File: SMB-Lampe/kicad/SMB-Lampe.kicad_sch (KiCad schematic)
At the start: 2 parts, among them P1 USB_C_Plug_USB2.0, SW1 SW_SPST

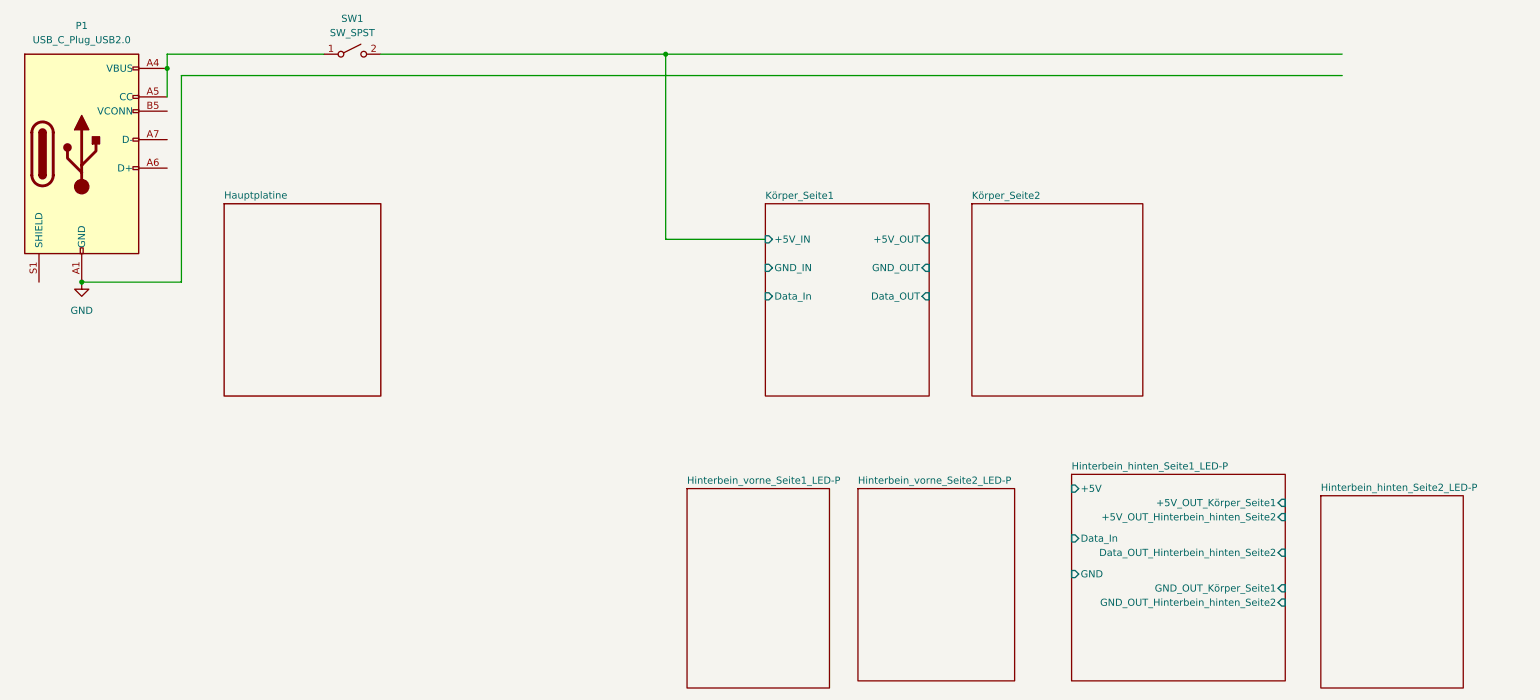
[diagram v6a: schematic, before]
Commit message: Vorderseite Platine Körper Seite 1 fertig
zwei GND Verbindungen fehlen noch
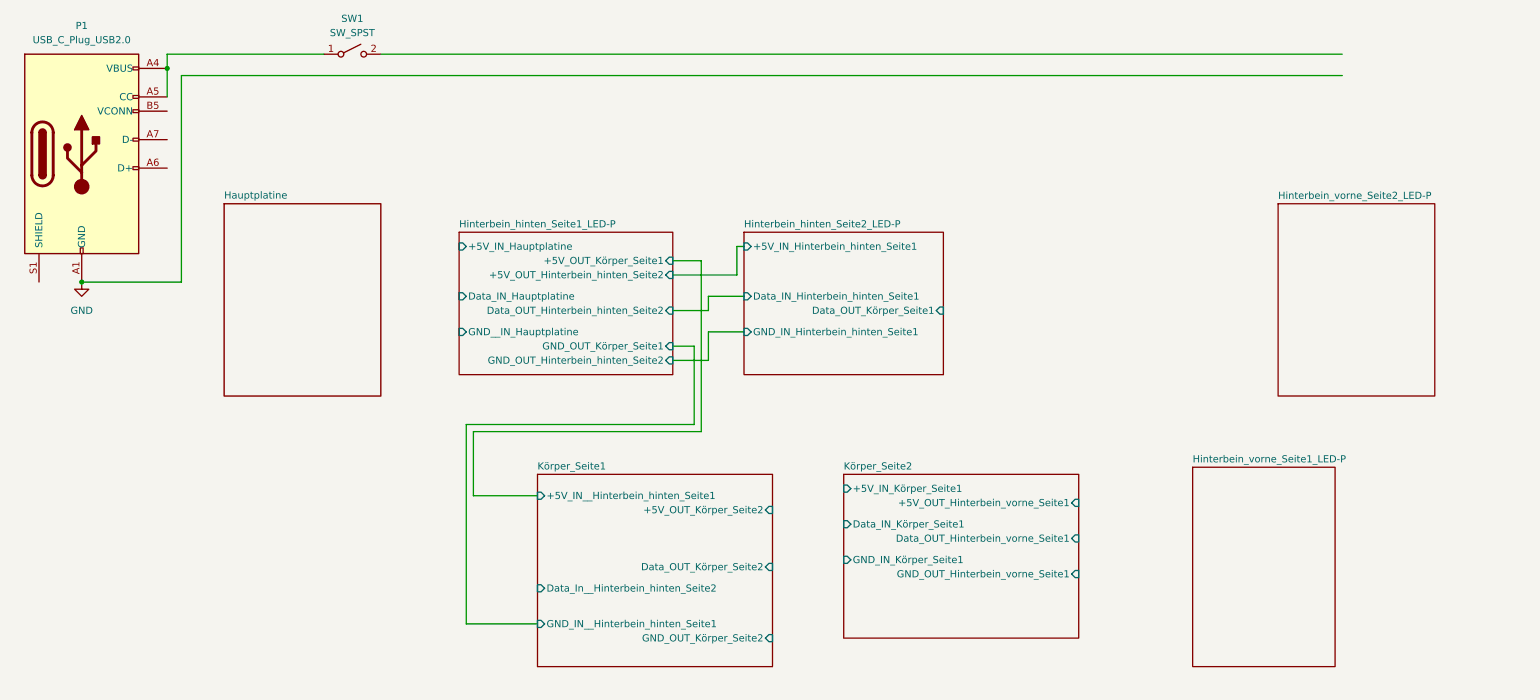
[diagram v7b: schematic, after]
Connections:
- net Körper_Seite1/+5V_IN: no longer names the net of SW1.2 (B)
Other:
- sheet Hinterbein_hinten_Seite1_LED-P ports: added +5V_IN_Hauptplatine, Data_IN_Hauptplatine, GND__IN_Hauptplatine; removed +5V, Data_In, GND
- sheet Hinterbein_hinten_Seite2_LED-P ports: added +5V_IN_Hinterbein_hinten_Seite1, Data_IN_Hinterbein_hinten_Seite1, Data_OUT_Körper_Seite1, GND_IN_Hinterbein_hinten_Seite1; removed none
- sheet Körper_Seite1 ports: added +5V_IN__Hinterbein_hinten_Seite1, +5V_OUT_Körper_Seite2, Data_In__Hinterbein_hinten_Seite2, Data_OUT_Körper_Seite2, GND_IN__Hinterbein_hinten_Seite1, GND_OUT_Körper_Seite2; removed +5V_IN, +5V_OUT, Data_In, Data_OUT, GND_IN, GND_OUT
- sheet Körper_Seite2 ports: added +5V_IN_Körper_Seite1, +5V_OUT_Hinterbein_vorne_Seite1, Data_IN_Körper_Seite1, Data_OUT_Hinterbein_vorne_Seite1, GND_IN_Körper_Seite1, GND_OUT_Hinterbein_vorne_Seite1; removed none

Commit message: Körper mit Vorder und Rückseite fertig
Alle Leiterbahnen sind gelegt und Verbindungen zu den anderen Platinen platziert
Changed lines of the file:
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@@
+	(wire
+		(pts
+			(xy 158.75 106.68) (xy 165.1 106.68)
+		)
+		(stroke
+			(width 0)
+			(type default)
+		)
+	)
 	(wire
 		(pts
@@
 	(wire
 		(pts
+			(xy 158.75 116.84) (xy 165.1 116.84)
+		)
+		(stroke
+			(width 0)
+			(type default)
+		)
+	)
+	(wire
+		(pts
 			(xy 144.78 91.44) (xy 104.14 91.44)
 		)
@@
 	(wire
 		(pts
+			(xy 165.1 106.68) (xy 165.1 102.87)
+		)
+		(stroke
+			(width 0)
+			(type default)
+		)
+	)
+	(wire
+		(pts
 			(xy 152.4 59.69) (xy 152.4 64.77)
 		)
@@
 	(wire
 		(pts
+			(xy 165.1 109.22) (xy 171.45 109.22)
+		)
+		(stroke
+			(width 0)
+			(type default)
+		)
+	)
+	(wire
+		(pts
 			(xy 140.97 77.47) (xy 144.78 77.47)
 		)
@@
 	(wire
 		(pts
+			(xy 158.75 129.54) (xy 166.37 129.54)
+		)
+		(stroke
+			(width 0)
+			(type default)
+		)
+	)
+	(wire
+		(pts
+			(xy 165.1 102.87) (xy 171.45 102.87)
+		)
+		(stroke
+			(width 0)
+			(type default)
+		)
+	)
+	(wire
+		(pts
 			(xy 50.8 27.94) (xy 50.8 33.02)
 		)
@@
 	(wire
 		(pts
+			(xy 166.37 129.54) (xy 166.37 115.57)
+		)
+		(stroke
+			(width 0)
+			(type default)
+		)
+	)
+	(wire
+		(pts
 			(xy 50.8 25.4) (xy 50.8 27.94)
 		)
@@
 	(wire
 		(pts
+			(xy 166.37 115.57) (xy 171.45 115.57)
+		)
+		(stroke
+			(width 0)
+			(type default)
+		)
+	)
+	(wire
+		(pts
 			(xy 147.32 74.93) (xy 153.67 74.93)
 		)
@@
 		(pts
 			(xy 152.4 59.69) (xy 153.67 59.69)
+		)
+		(stroke
+			(width 0)
+			(type default)
+		)
+	)
+	(wire
+		(pts
+			(xy 165.1 116.84) (xy 165.1 109.22)
 		)
 		(stroke
@@
 		)
 		(pin "Data_In__Hinterbein_hinten_Seite2" input
-			(at 116.84 120.65 180)
-			(effects
-				(font
+			(at 116.84 114.3 180)
+			(effects
+				(font
